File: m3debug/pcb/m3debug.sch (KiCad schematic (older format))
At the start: 52 parts

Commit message: Route most of m3debug
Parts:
- removed R? (x10): R, symbol R
- removed SW?: SUPPLY_POWER, symbol SWITCH_DPDT
- added C14, C18: 10µ, agg:0603, symbol C
- added C16: 1n, agg:0402, symbol C
- added D12, D13: RED, agg:0603-LED, symbol LED
- added J7: PYRO1, agg:B02B-PASK, symbol CONN_01x02
- added R1, R10, R11, R12, R13, R14, R15, R16, R17, R18, R7, R8, R9: 1k, agg:0402, symbol R
- added R3: 4k7, agg:0402, symbol R
- added R4: 10k, agg:0402, symbol R
- added SW3: SUPPLY_5V, agg:A101SYCQ04, symbol SWITCH_SPDT
- added SW4: SUPPLY_3V3, agg:A101SYCQ04, symbol SWITCH_SPDT
- C15, C17: renamed from C?; value C -> 2µ2; footprint (none) -> agg:0603
- D1, D2, D3, D4, D5, D6, D7, D8, D9: renamed from D?; footprint (none) -> agg:0603-LED
- D10, D11: renamed from D?; value GRN -> YLW; footprint (none) -> agg:0603-LED
- J6: renamed from J?; value CONN_01x02 -> CHARGING; footprint (none) -> agg:B02B-PASK
- R5: renamed from R?; footprint (none) -> agg:0402
- R6: renamed from R?; value R -> 1k; footprint (none) -> agg:0402; Farnell (none) -> 9232761
- SW1, SW2: renamed from SW?; footprint (none) -> agg:A101SYCQ04; Farnell (none) -> 2292959
- gave numbers to parts that had none: 23
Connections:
- net labels added: LED0, LED1, LED2, TPWR_MON
- wire segments 253 -> 284
- no-connect marks 47 -> 41
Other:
- moved on the sheet: C17, D10, D11, D2, D3, D4, D5, D6, D7, D8, D9, J5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

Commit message: update m3debug to be much more useful
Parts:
- removed D1, D2: GRN, agg:0603-LED, symbol LED
- removed D13: RED, agg:0603-LED, symbol LED
- removed J6: CHARGING, agg:B02B-PASK, symbol CONN_01x02
- removed J7: PYRO1, agg:B02B-PASK, symbol CONN_01x02
- removed R18, R6, R7: 1k, agg:0402, symbol R
- removed SW1: PYRO_ARMING, agg:A101SYCQ04, symbol SWITCH_SPDT
- removed SW2: POWER_SWITCH, agg:A101SYCQ04, symbol SWITCH_SPDT
- removed SW3: SUPPLY_5V, agg:A101SYCQ04, symbol SWITCH_SPDT
- removed SW4: SUPPLY_3V3, agg:A101SYCQ04, symbol SWITCH_SPDT
- added D8: RED, agg:0603-LED, symbol LED
- added D9: GRN, agg:0603-LED, symbol LED
- added J10: CONN_02x05, agg:DIL-254P-10, symbol CONN_02x05
- added J11, J13, J7: CONN_02x01, agg:SIL-254P-02, symbol CONN_02x01
- added J12: CONN_02x07, agg:DIL-254P-14, symbol CONN_02x07
- added J5, J8: CONN_01x02, agg:S02B-PASK-2, symbol CONN_01x02
- added J6: CONN_02x04, agg:DIL-254P-08, symbol CONN_02x04
- added R13, R14: 1k, agg:0402, symbol R
- renumbered C15 to C13, C16 to C14, C17 to C15, C18 to C16, C14 to C17, D10 to D1, D8 to D10, D7 to D11, D9 to D12, D11 to D2, D12 to D3, D3 to D4, D4 to D5, D5 to D6, D6 to D7, J5 to J9, R15 to R1, R9 to R10, R10 to R11, R11 to R12, R13 to R15, R12 to R16, R14 to R17, R16 to R2, R17 to R3, R1 to R4, R2 to R5, R5 to R6, R3 to R7, R4 to R8, R8 to R9
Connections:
- wire segments 284 -> 301
- no-connect marks 41 -> 37
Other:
- note added: "POWER MANAGEMENT"
- note added: "PSU SUPPORT"
- note added: "PYRO SUPPORT"
- note removed: "POWER/CONNECTORS"
- note removed: "USER INTERFACE"
- moved on the sheet: C1, C10, C11, C13, C14, C15, C16, C17, C2, C3, C4, C5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

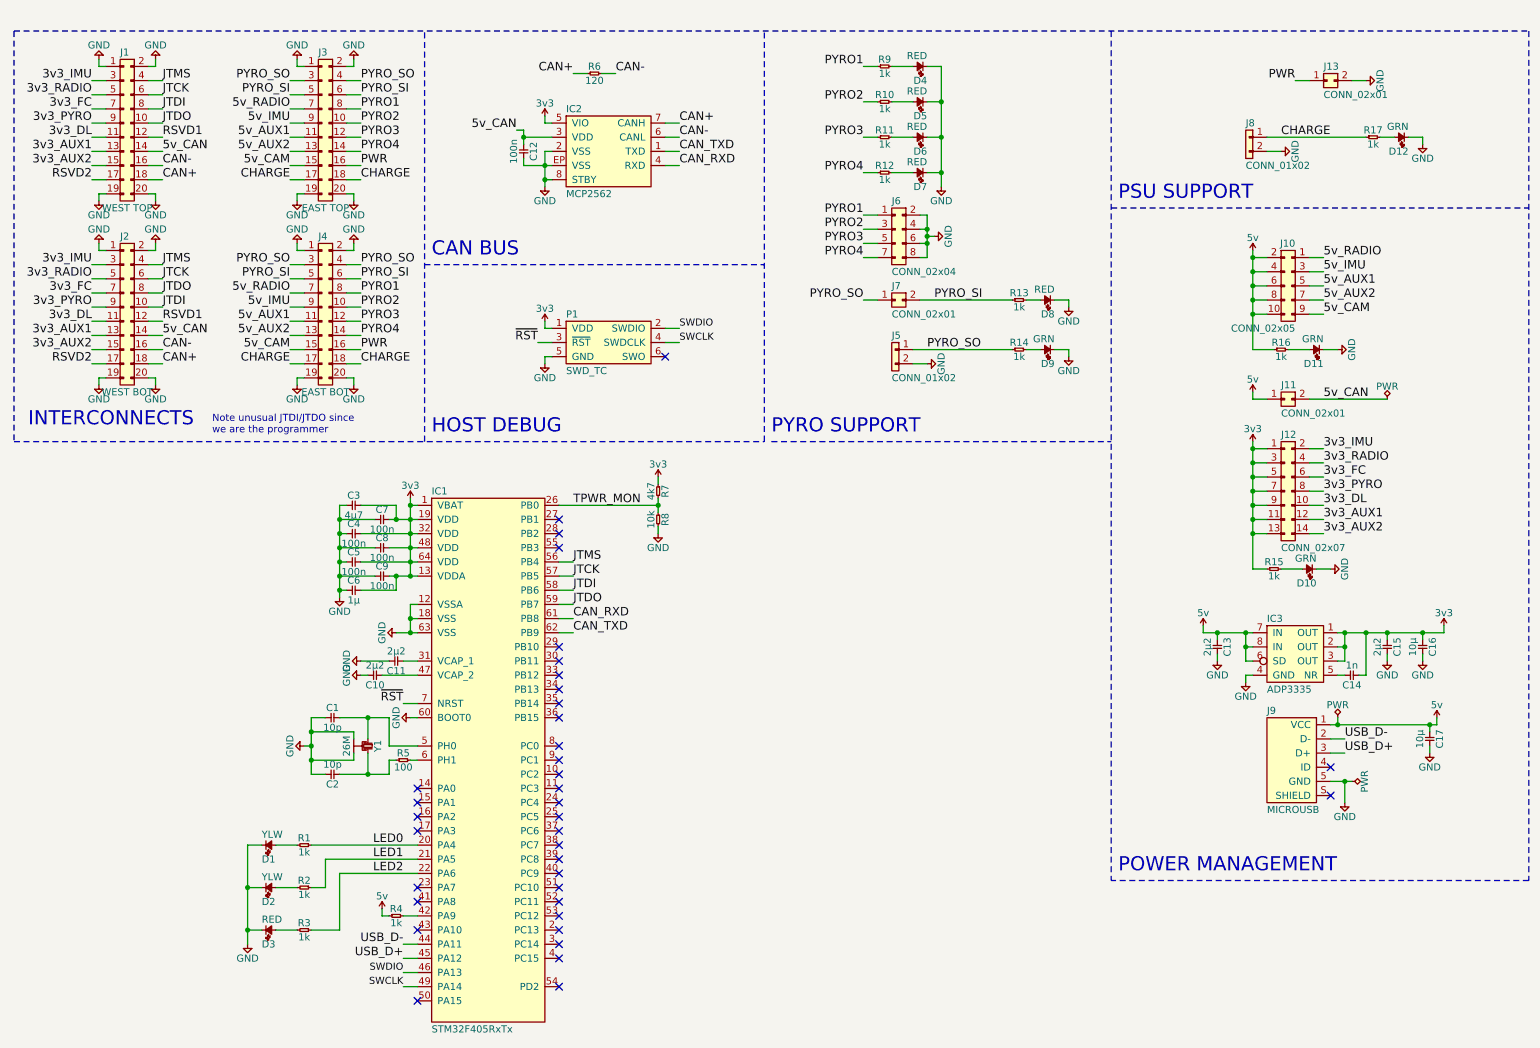
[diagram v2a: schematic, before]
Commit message: route a lot of m3debug
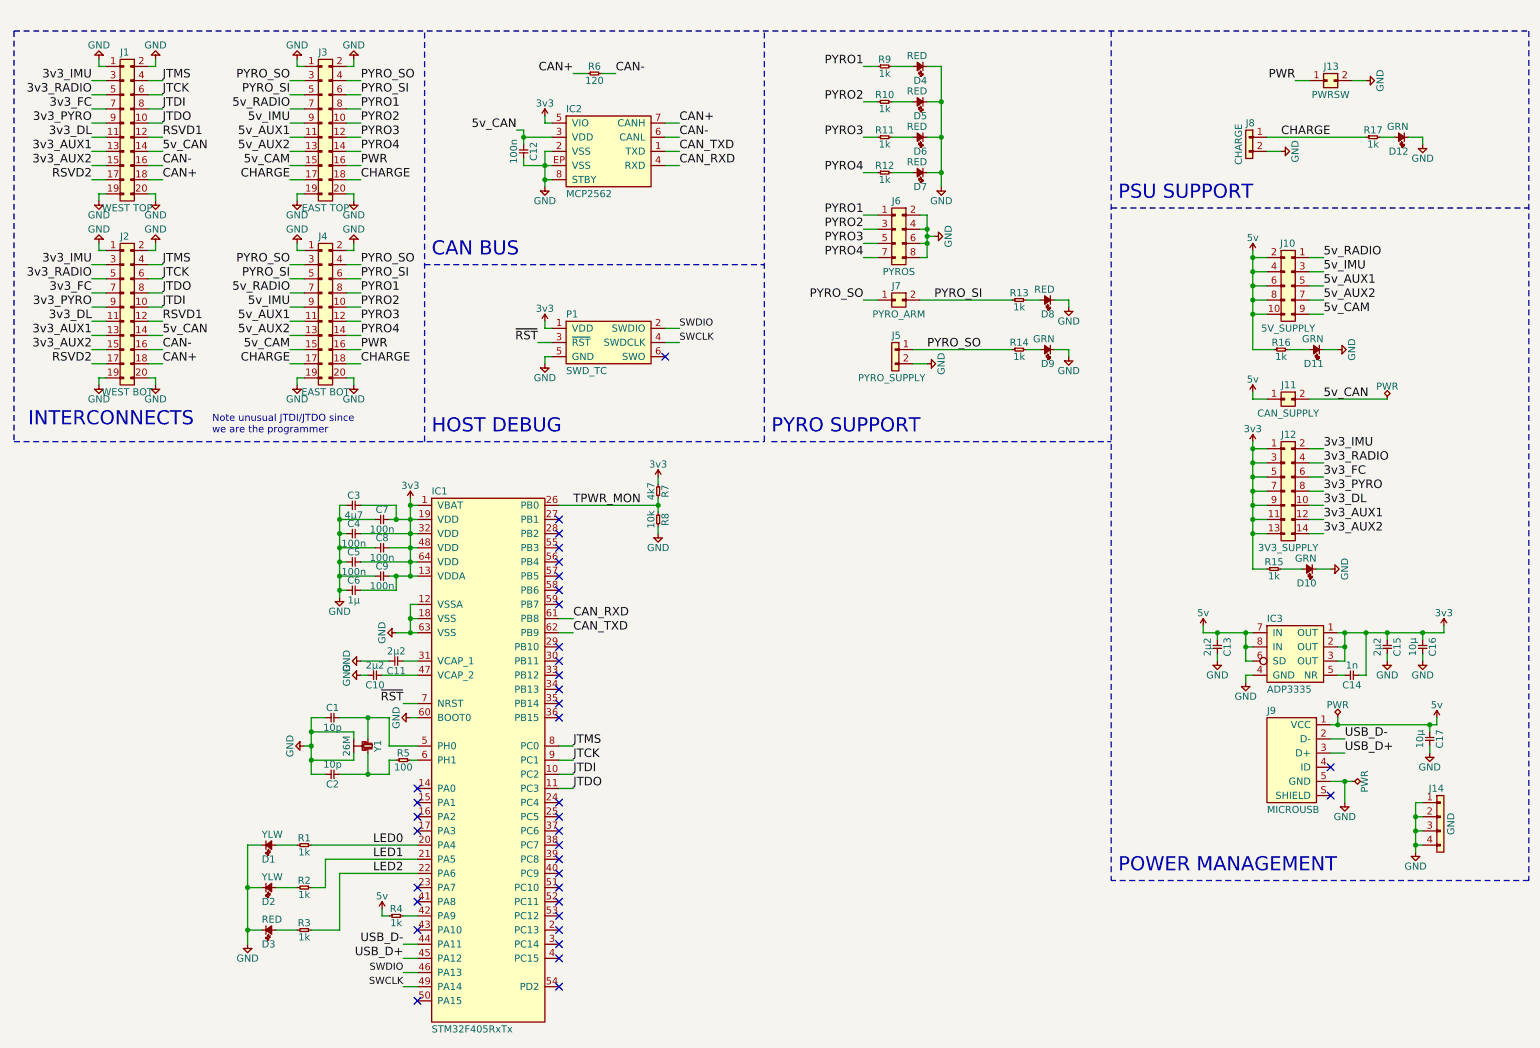
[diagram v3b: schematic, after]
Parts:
- added J14: GND, agg:SIL-254P-04, symbol CONN_01x04
- J10: value CONN_02x05 -> 5V_SUPPLY
- J11: value CONN_02x01 -> CAN_SUPPLY
- J12: value CONN_02x07 -> 3V3_SUPPLY
- J13: value CONN_02x01 -> PWRSW
- J5: value CONN_01x02 -> PYRO_SUPPLY
- J6: value CONN_02x04 -> PYROS
- J7: value CONN_02x01 -> PYRO_ARM
- J8: value CONN_01x02 -> CHARGE
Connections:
- net GND: now also J14.1, J14.2, J14.3, J14.4
- net JTCK: now also IC1.9 (PC1); no longer IC1.57 (PB5)
- net JTDI: now also IC1.10 (PC2); no longer IC1.58 (PB6)
- net JTDO: now also IC1.11 (PC3); no longer IC1.59 (PB7)
- net JTMS: now also IC1.8 (PC0); no longer IC1.56 (PB4)
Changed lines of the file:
@@
 NoConn ~ 4350 6250
 NoConn ~ 4350 6050
-NoConn ~ 4350 5850
-NoConn ~ 4350 5750
-NoConn ~ 4350 5650
-NoConn ~ 4350 5550
 NoConn ~ 4350 3950
 NoConn ~ 4350 5950
@@
 	-1   0    0    1
 $EndComp
-Text Label 4450 4450 0    60   ~ 0
+Text Label 4450 5750 0    60   ~ 0
 JTDI
-Text Label 4450 4250 0    60   ~ 0
+Text Label 4450 5550 0    60   ~ 0
 JTMS
-Text Label 4450 4350 0    60   ~ 0
+Text Label 4450 5650 0    60   ~ 0
 JTCK
-Text Label 4450 4550 0    60   ~ 0
+Text Label 4450 5850 0    60   ~ 0
 JTDO
 Text Label 1550 1050 0    60   ~ 0
@@
 P 9850 850
 F 0 "J13" H 9750 950 50  0000 L CNN
-F 1 "CONN_02x01" H 9750 750 50  0000 L CNN
+F 1 "PWRSW" H 9800 750 50  0000 C CNN
 F 2 "agg:SIL-254P-02" H 9850 850 50  0001 C CNN
 F 3 "" H 9850 850 50  0001 C CNN
@@
 P 6800 2400
 F 0 "J7" H 6700 2500 50  0000 L CNN
-F 1 "CONN_02x01" H 6700 2300 50  0000 L CNN
+F 1 "PYRO_ARM" H 6750 2300 50  0000 C CNN
 F 2 "agg:SIL-254P-02" H 6800 2400 50  0001 C CNN
 F 3 "" H 6800 2400 50  0001 C CNN
@@
 P 6800 1800
 F 0 "J6" H 6700 1900 50  0000 L CNN
-F 1 "CONN_02x04" H 6700 1400 50  0000 L CNN
+F 1 "PYROS" H 6750 1400 50  0000 C CNN
 F 2 "agg:DIL-254P-08" H 6800 1800 50  0001 C CNN
 F 3 "" H 6800 1800 50  0001 C CNN
@@
 P 9250 1250
 F 0 "J8" H 9200 1350 50  0000 L CNN
-F 1 "CONN_01x02" H 9200 1050 50  0000 L CNN
+F 1 "CHARGE" V 9150 1200 50  0000 C CNN
 F 2 "agg:S02B-PASK-2" H 9250 1250 50  0001 C CNN
 F 3 "" H 9250 1250 50  0001 C CNN
@@
 P 6750 2750
 F 0 "J5" H 6700 2850 50  0000 L CNN
-F 1 "CONN_01x02" H 6700 2550 50  0000 L CNN
+F 1 "PYRO_SUPPLY" H 6700 2550 50  0000 C CNN
 F 2 "agg:S02B-PASK-2" H 6750 2750 50  0001 C CNN
 F 3 "" H 6750 2750 50  0001 C CNN
@@
 Connection ~ 5050 3850
 Wire Wire Line
-	4350 4550 4450 4550
-Wire Wire Line
-	4450 4450 4350 4450
-Wire Wire Line
-	4350 4350 4450 4350
-Wire Wire Line
-	4450 4250 4350 4250
-Wire Wire Line
 	2700 6350 3350 6350
 Wire Wire Line
@@
 P 9450 2100
 F 0 "J10" H 9350 2200 50  0000 L CNN
-F 1 "CONN_02x05" H 9350 1600 50  0000 L CNN
+F 1 "5V_SUPPLY" H 9400 1600 50  0000 C CNN
 F 2 "agg:DIL-254P-10" H 9450 2100 50  0001 C CNN
 F 3 "" H 9450 2100 50  0001 C CNN
@@
 P 9550 3450
 F 0 "J12" H 9450 3550 50  0000 L CNN
-F 1 "CONN_02x07" H 9450 2750 50  0000 L CNN
+F 1 "3V3_SUPPLY" H 9500 2750 50  0000 C CNN
 F 2 "agg:DIL-254P-14" H 9550 3450 50  0001 C CNN
 F 3 "" H 9550 3450 50  0001 C CNN
@@
 P 9550 3100
 F 0 "J11" H 9450 3200 50  0000 L CNN
-F 1 "CONN_02x01" H 9450 3000 50  0000 L CNN
+F 1 "CAN_SUPPLY" H 9500 3000 50  0000 C CNN
 F 2 "agg:SIL-254P-02" H 9550 3100 50  0001 C CNN
 F 3 "" H 9550 3100 50  0001 C CNN
@@
 	1    0    0    -1
 $EndComp
+$Comp
+L CONN_01x04 J14
+U 1 1 56C3FE03
+P 10550 5950
+F 0 "J14" H 10500 6050 50  0000 L CNN
+F 1 "GND" V 10450 5800 50  0000 C CNN
+F 2 "agg:SIL-254P-04" H 10550 5950 50  0001 C CNN
+F 3 "" H 10550 5950 50  0001 C CNN
+	1    10550 5950
+	-1   0    0    -1
+$EndComp
+$Comp
+L GND #PWR057
+U 1 1 56C4087C
+P 10400 6300
+F 0 "#PWR057" H 10270 6340 50  0001 L CNN
+F 1 "GND" H 10400 6200 50  0000 C CNN
+F 2 "" H 10400 6300 60  0000 C CNN
+F 3 "" H 10400 6300 60  0000 C CNN
+	1    10400 6300
+	1    0    0    -1
+$EndComp
+Wire Wire Line
+	10450 5950 10400 5950
+Wire Wire Line
+	10400 5950 10400 6300
+Wire Wire Line
+	10450 6250 10400 6250
+Connection ~ 10400 6250
+Wire Wire Line
+	10400 6150 10450 6150
+Connection ~ 10400 6150
+Wire Wire Line
+	10450 6050 10400 6050
+Connection ~ 10400 6050
+NoConn ~ 4350 4250
+NoConn ~ 4350 4350
+NoConn ~ 4350 4450
+NoConn ~ 4350 4550
+Wire Wire Line
+	4450 5550 4350 5550
+Wire Wire Line
+	4350 5650 4450 5650
+Wire Wire Line
+	4450 5750 4350 5750
+Wire Wire Line
+	4350 5850 4450 5850
 $EndSCHEMATC

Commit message: add some farnell bom lines
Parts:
- C13, C15: Farnell (none) -> 2496923
- D1, D2: Farnell (none) -> 2290330
- D10, D11, D12, D9: Farnell (none) -> 2290328
- D3, D4, D5, D6, D7, D8: Farnell (none) -> 2290329
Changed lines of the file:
@@
 F 2 "agg:0603-LED" H 6950 750 50  0001 C CNN
 F 3 "" H 6950 750 50  0001 C CNN
+F 4 "2290329" H 6950 750 60  0001 C CNN "Farnell"
 	1    6950 750
 	-1   0    0    1
@@
 F 2 "agg:0603-LED" H 6950 1000 50  0001 C CNN
 F 3 "" H 6950 1000 50  0001 C CNN
+F 4 "2290329" H 6950 1000 60  0001 C CNN "Farnell"
 	1    6950 1000
 	-1   0    0    1
@@
 F 2 "agg:0603-LED" H 6950 1250 50  0001 C CNN
 F 3 "" H 6950 1250 50  0001 C CNN
+F 4 "2290329" H 6950 1250 60  0001 C CNN "Farnell"
 	1    6950 1250
 	-1   0    0    1
@@
 F 2 "agg:0603-LED" H 6950 1500 50  0001 C CNN
 F 3 "" H 6950 1500 50  0001 C CNN
+F 4 "2290329" H 6950 1500 60  0001 C CNN "Farnell"
 	1    6950 1500
 	-1   0    0    1
@@
 F 2 "agg:0603-LED" H 9750 2750 50  0001 C CNN
 F 3 "" H 9750 2750 50  0001 C CNN
+F 4 "2290328" H 9750 2750 60  0001 C CNN "Farnell"
 	1    9750 2750
 	-1   0    0    1
@@
 F 2 "agg:0603" H 10200 4800 50  0001 C CNN
 F 3 "" H 10200 4800 50  0001 C CNN
+F 4 "2496923" H 10200 4800 60  0001 C CNN "Farnell"
 	1    10200 4800
 	0    1    1    0
@@
 F 2 "agg:0603" H 9000 4800 50  0001 C CNN
 F 3 "" H 9000 4800 50  0001 C CNN
+F 4 "2496923" H 9000 4800 60  0001 C CNN "Farnell"
 	1    9000 4800
 	0    1    1    0
@@
 F 2 "agg:0603-LED" H 10350 1250 50  0001 C CNN
 F 3 "" H 10350 1250 50  0001 C CNN
+F 4 "2290328" H 10350 1250 60  0001 C CNN "Farnell"
 	1    10350 1250
 	-1   0    0    1
@@
 F 2 "agg:0603-LED" H 9700 4300 50  0001 C CNN
 F 3 "" H 9700 4300 50  0001 C CNN
+F 4 "2290328" H 9700 4300 60  0001 C CNN "Farnell"
 	1    9700 4300
 	-1   0    0    1
@@
 F 2 "agg:0603-LED" H 2250 6550 50  0001 C CNN
 F 3 "" H 2250 6550 50  0001 C CNN
+F 4 "2290330" H 2250 6550 60  0001 C CNN "Farnell"
 	1    2250 6550
 	1    0    0    1
@@
 F 2 "agg:0603-LED" H 2250 6250 50  0001 C CNN
 F 3 "" H 2250 6250 50  0001 C CNN
+F 4 "2290330" H 2250 6250 60  0001 C CNN "Farnell"
 	1    2250 6250
 	1    0    0    1
@@
 F 2 "agg:0603-LED" H 2250 6850 50  0001 C CNN
 F 3 "" H 2250 6850 50  0001 C CNN
+F 4 "2290329" H 2250 6850 60  0001 C CNN "Farnell"
 	1    2250 6850
 	1    0    0    1
@@
 F 2 "agg:0603-LED" H 7850 2400 50  0001 C CNN
 F 3 "" H 7850 2400 50  0001 C CNN
+F 4 "2290329" H 7850 2400 60  0001 C CNN "Farnell"
 	1    7850 2400
 	-1   0    0    1
@@
 F 2 "agg:0603-LED" H 7850 2750 50  0001 C CNN
 F 3 "" H 7850 2750 50  0001 C CNN
+F 4 "2290328" H 7850 2750 60  0001 C CNN "Farnell"
 	1    7850 2750
 	-1   0    0    1

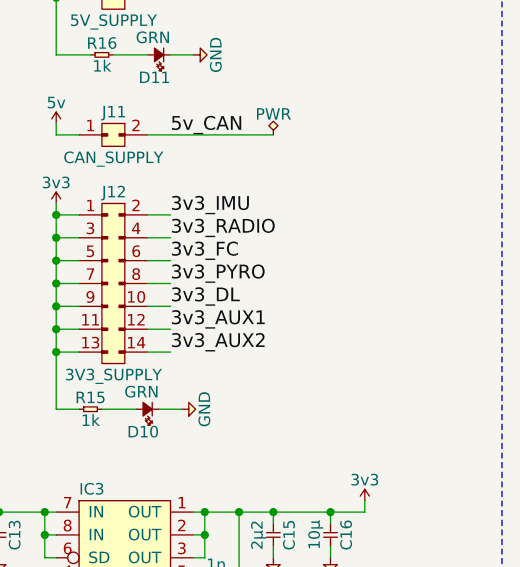
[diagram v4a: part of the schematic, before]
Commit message: finish bom for m3debug
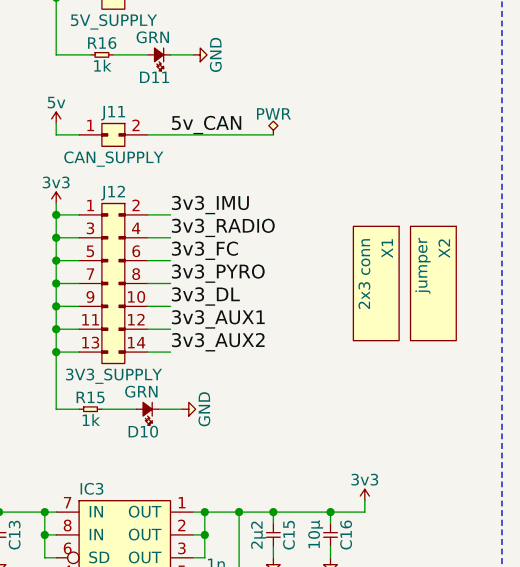
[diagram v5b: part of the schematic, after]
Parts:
- added X1: 2x3 conn, symbol PART
- added X2: jumper, symbol PART
- C14: Farnell (none) -> 2496767
- C16, C17: Farnell (none) -> 2456110
- J10: Farnell (none) -> 1022235
- J11, J13, J7: Farnell (none) -> 1022245
- J12, J6: Farnell (none) -> 1022232
- J14: Farnell (none) -> 1022250
- J5, J8: Farnell (none) -> 1830747
- R6: Farnell (none) -> 2072575
- R7: Farnell (none) -> 1358060
- R8: Farnell (none) -> 1358069
